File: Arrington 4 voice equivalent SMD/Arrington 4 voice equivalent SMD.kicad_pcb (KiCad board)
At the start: 2 copper layers, 31.8 x 40.1 mm, 21 parts, among them J1 SJ1-3525N, J2 DB25_Male, J3 RCJ-013, SW1 SW_SPDT, U1 74LS05, U2 74LS05

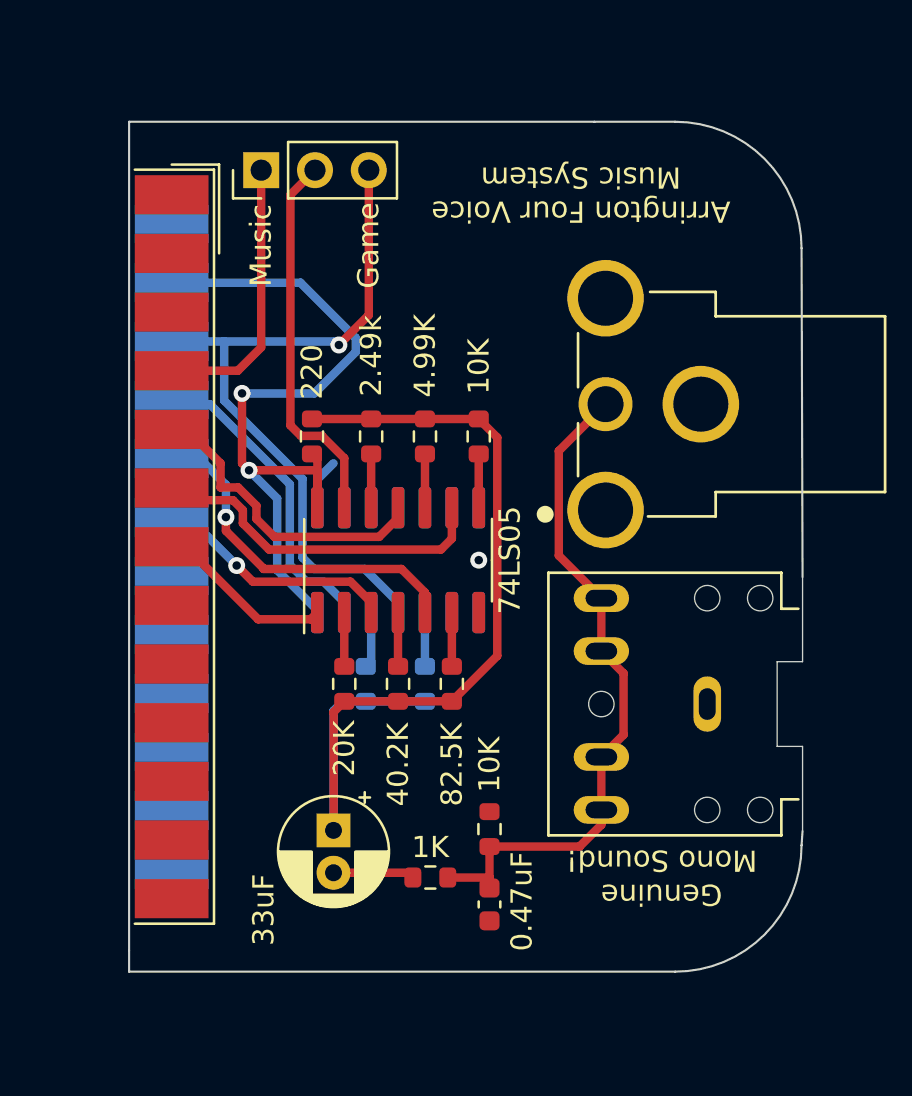
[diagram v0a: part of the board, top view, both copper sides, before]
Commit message: removed outdated gerbers, updated design to version 2
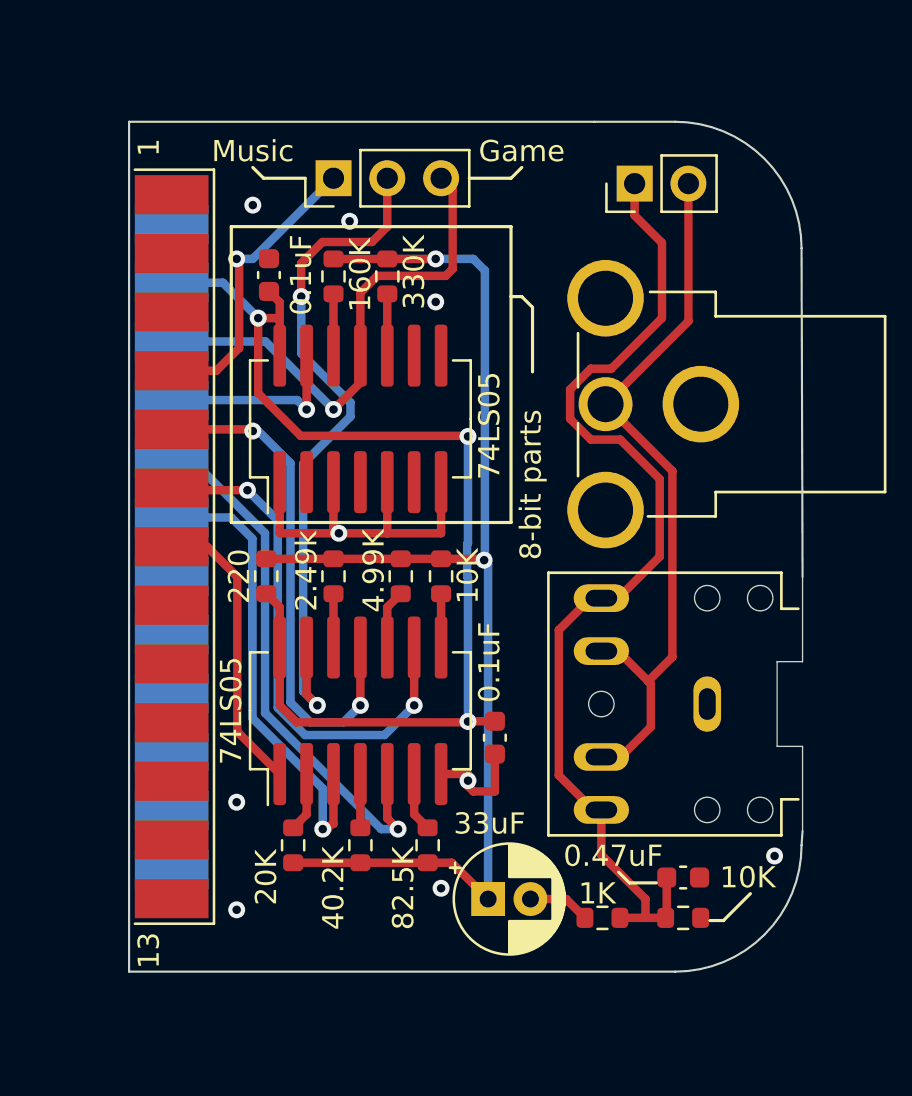
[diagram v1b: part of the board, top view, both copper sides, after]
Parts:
- added C3: 0.1uF, Capacitor_SMD:C_0603_1608Metric, F.Cu at (127.0, 82.5)
- added C4: 0.1uF, Capacitor_SMD:C_0603_1608Metric, F.Cu at (116.3, 60.7)
- added J4: disable connector switch, Connector_PinHeader_2.54mm:PinHeader_1x02_P2.54mm_Vertical, F.Cu at (133.6, 56.4)
- R10: value bit 0 -> 330K; moved to F.Cu
- R11: value bit 1 -> 160K; moved to F.Cu
- U1: footprint Package_SO:SO-14_3.9x8.65mm_P1.27mm -> Evan's parts:SO-14_5.3x10.2mm_P1.27mm double footprint
- U2: footprint Package_SO:SO-14_3.9x8.65mm_P1.27mm -> Evan's parts:SO-14_5.3x10.2mm_P1.27mm double footprint; moved to F.Cu
- moved R10 19.3 mm to (121.9, 60.8), turned to -90 degrees
- moved R11 19.3 mm to (119.4, 60.8), turned to -90 degrees
- moved G*** 16.6 mm to (137.7, 62.0)
- moved G*** 11.2 mm to (137.7, 89.7)
- moved R1 10.1 mm to (135.9, 91.1), turned to 0 degrees
- moved C1 9.23 mm to (135.9, 89.2), turned to 0 degrees
- moved R2 8.35 mm to (132.1, 91.1)
- moved R3 7.99 mm to (117.5, 87.6)
- moved C2 7.99 mm to (126.7, 90.2), turned to 0 degrees
- moved R4 7.82 mm to (120.7, 87.6)
- moved R6 7.71 mm to (123.8, 87.6)
- moved U1 7.33 mm to (120.7, 81.3)
- moved R9 6.95 mm to (116.2, 74.9)
- moved U2 6.90 mm to (120.7, 67.5), turned to 90 degrees
- moved R5 6.84 mm to (124.5, 74.9)
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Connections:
- C1 pad 1: Net-(C1-Pad1) -> Net-(J4-Pin_1)
- J1 pad 10: Net-(C1-Pad1) -> Net-(J4-Pin_2)
- J1 pad 11: Net-(C1-Pad1) -> Net-(J4-Pin_2)
- J1 pad 2: Net-(C1-Pad1) -> Net-(J4-Pin_1)
- J1 pad 3: Net-(C1-Pad1) -> Net-(J4-Pin_1)
- J3 pad 2: Net-(C1-Pad1) -> Net-(J4-Pin_2)
- R1 pad 1: Net-(C1-Pad1) -> Net-(J4-Pin_1)
- R2 pad 1: Net-(C1-Pad1) -> Net-(J4-Pin_1)
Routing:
- net Net-(J4-Pin_1): track 0.00 -> 48.9 mm
- net Net-(J4-Pin_2): track 0.00 -> 34.8 mm
- net Net-(C1-Pad1): track 32.1 -> 0.00 mm
- net GND: track 2.41 -> 22.4 mm, vias 1 -> 9
- net VCC: track 36.1 -> 52.9 mm, vias 2 -> 3
- net Net-(SW1-B): track 18.1 -> 33.1 mm, vias 0 -> 2
- net /mixed audio: track 44.0 -> 57.5 mm, vias 0 -> 2
- net Net-(J2-P19): track 11.6 -> 22.5 mm
- net /bit 0: track 34.4 -> 24.3 mm
- net Net-(J2-Pad5): track 14.7 -> 24.3 mm, vias 0 -> 2
- net Net-(J2-P18): track 16.8 -> 25.7 mm
- net Net-(J2-Pad6): track 16.5 -> 24.8 mm, vias 0 -> 2
- net /bit 1: track 14.8 -> 9.10 mm, vias 0 -> 1
- net Net-(J2-Pad7): track 8.43 -> 13.8 mm
- net /bit 7: track 13.1 -> 14.2 mm, vias 0 -> 1
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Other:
- board text added: "1"
- board text added: "13"
- board text added: "14"
- board text added: "25"
- board text added: "8-bit parts"
- board text added: "Jumper for simultaneous RCA and TRS output"
- board text added: "SMD Ver. 2"
- board text added: "slide switch"
- board text removed: "Good luck with the resistor values!"
- board text removed: "Populate back components for optional 8-bit sound"
